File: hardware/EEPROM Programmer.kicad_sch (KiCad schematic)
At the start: 4 parts, among them U1 74HCT164, U2 74HCT164, U3 Teensy2.0_(Arduino)

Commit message: add power LED
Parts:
- added D1: LED, LED_THT:LED_D3.0mm, symbol Device:LED
- added R1: 2k2, Resistor_THT:R_Axial_DIN0207_L6.3mm_D2.5mm_P7.62mm_Horizontal, symbol Device:R
- renumbered 1 to 11
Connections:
- net +5V: now also R1.1
- net GND: now also D1.1 (K)
- new net: D1.2 (A), R1.2
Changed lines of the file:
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@@
     (pin "1")
+  )
+  (symbol (lib_id "Device:LED") (at 58.42 48.26 180) (unit 1)
+    (in_bom yes) (on_board yes) (fields_autoplaced)
+    (property "Reference" "D1" (id 0) (at 60.0075 40.64 0))
+    (property "Value" "LED" (id 1) (at 60.0075 43.18 0))
+    (property "Footprint" "LED_THT:LED_D3.0mm" (id 2) (at 58.42 48.26 0)
+      (effects (font (size 1.27 1.27)) hide)
+    )
+    (property "Datasheet" "~" (id 3) (at 58.42 48.26 0)
+      (effects (font (size 1.27 1.27)) hide)
+    )
+    (pin "1")
+    (pin "2")
   )
   (symbol (lib_id "power:+5V") (at 113.03 74.93 0) (unit 1)
@@
     (pin "9")
   )
+  (symbol (lib_id "power:GND") (at 62.23 48.26 90) (unit 1)
+    (in_bom yes) (on_board yes) (fields_autoplaced)
+    (property "Reference" "#PWR02" (id 0) (at 68.58 48.26 0)
+      (effects (font (size 1.27 1.27)) hide)
+    )
+    (property "Value" "GND" (id 1) (at 66.04 48.2599 90)
+      (effects (font (size 1.27 1.27)) (justify right))
+    )
+    (property "Footprint" "" (id 2) (at 62.23 48.26 0)
+      (effects (font (size 1.27 1.27)) hide)
+    )
+    (property "Datasheet" "" (id 3) (at 62.23 48.26 0)
+      (effects (font (size 1.27 1.27)) hide)
+    )
+    (pin "1")
+  )
   (symbol (lib_id "power:GND") (at 113.03 102.87 0) (unit 1)
     (in_bom yes) (on_board yes) (fields_autoplaced)
@@
     (pin "1")
   )
+  (symbol (lib_id "power:+5V") (at 46.99 48.26 90) (unit 1)
+    (in_bom yes) (on_board yes) (fields_autoplaced)
+    (property "Reference" "#PWR01" (id 0) (at 50.8 48.26 0)
+      (effects (font (size 1.27 1.27)) hide)
+    )
+    (property "Value" "+5V" (id 1) (at 43.18 48.2599 90)
+      (effects (font (size 1.27 1.27)) (justify left))
+    )
+    (property "Footprint" "" (id 2) (at 46.99 48.26 0)
+      (effects (font (size 1.27 1.27)) hide)
+    )
+    (property "Datasheet" "" (id 3) (at 46.99 48.26 0)
+      (effects (font (size 1.27 1.27)) hide)
+    )
+    (pin "1")
+  )
   (symbol (lib_id "28-6553-10_:28-6553-10_") (at 180.34 87.63 0) (unit 1)
-    (in_bom yes) (on_board yes) (fields_autoplaced)
-    (property "Reference" "1" (id 0) (at 232.41 78.2193 0))
-    (property "Value" "28-6553-10_" (id 1) (at 232.41 80.7593 0))
+    (in_bom yes) (on_board yes)
+    (property "Reference" "11" (id 0) (at 232.41 78.2193 0))
+    (property "Value" "28-6553-10_" (id 1) (at 232.41 81.28 0))
     (property "Footprint" "aries_zif:28655310" (id 2) (at 180.34 87.63 0)
       (effects (font (size 1.27 1.27)) hide)
@@
     )
     (property "Reference_1" "J" (id 4) (at 232.41 83.2993 0))
-    (property "Value_1" "28-6553-10_" (id 5) (at 232.41 85.8393 0))
+    (property "Value_1" "28-6553-10_" (id 5) (at 232.41 86.36 0))
     (property "Footprint_1" "28655310" (id 6) (at 224.79 177.47 0)
       (effects (font (size 1.27 1.27)) (justify left top) hide)
@@
     (pin "1")
   )
+  (symbol (lib_id "Device:R") (at 50.8 48.26 90) (unit 1)
+    (in_bom yes) (on_board yes) (fields_autoplaced)
+    (property "Reference" "R1" (id 0) (at 50.8 41.91 90))
+    (property "Value" "2k2" (id 1) (at 50.8 44.45 90))
+    (property "Footprint" "Resistor_THT:R_Axial_DIN0207_L6.3mm_D2.5mm_P7.62mm_Horizontal" (id 2) (at 50.8 50.038 90)
+      (effects (font (size 1.27 1.27)) hide)
+    )
+    (property "Datasheet" "~" (id 3) (at 50.8 48.26 0)
+      (effects (font (size 1.27 1.27)) hide)
+    )
+    (pin "1")
+    (pin "2")
+  )
   (sheet_instances
     (path "/" (page "1"))
   )
   (symbol_instances
+    (path "/c63c60b6-cef6-4c5a-8281-c9ca3487848c"
+      (reference "#PWR01") (unit 1) (value "+5V") (footprint "")
+    )
+    (path "/a79ec797-6aff-42a3-aa50-ffe5540c9212"
+      (reference "#PWR02") (unit 1) (value "GND") (footprint "")
+    )
     (path "/45c3618f-0671-416b-9a91-eff4d1eef6eb"
       (reference "#PWR0101") (unit 1) (value "GND") (footprint "")
@@
     )
     (path "/c9991c46-c0f1-40b8-b89b-d80d88dbb5f5"
-      (reference "1") (unit 1) (value "28-6553-10_") (footprint "aries_zif:28655310")
+      (reference "11") (unit 1) (value "28-6553-10_") (footprint "aries_zif:28655310")
+    )
+    (path "/79b34c4a-e5fe-43e9-8c64-054d107017f5"
+      (reference "D1") (unit 1) (value "LED") (footprint "LED_THT:LED_D3.0mm")
+    )
+    (path "/f85433e7-6fd8-482d-8fd4-e22dd35dd3ac"
+      (reference "R1") (unit 1) (value "2k2") (footprint "Resistor_THT:R_Axial_DIN0207_L6.3mm_D2.5mm_P7.62mm_Horizontal")
     )
     (path "/51f0c9ae-1fd9-4c54-9533-3dafdaf38498"

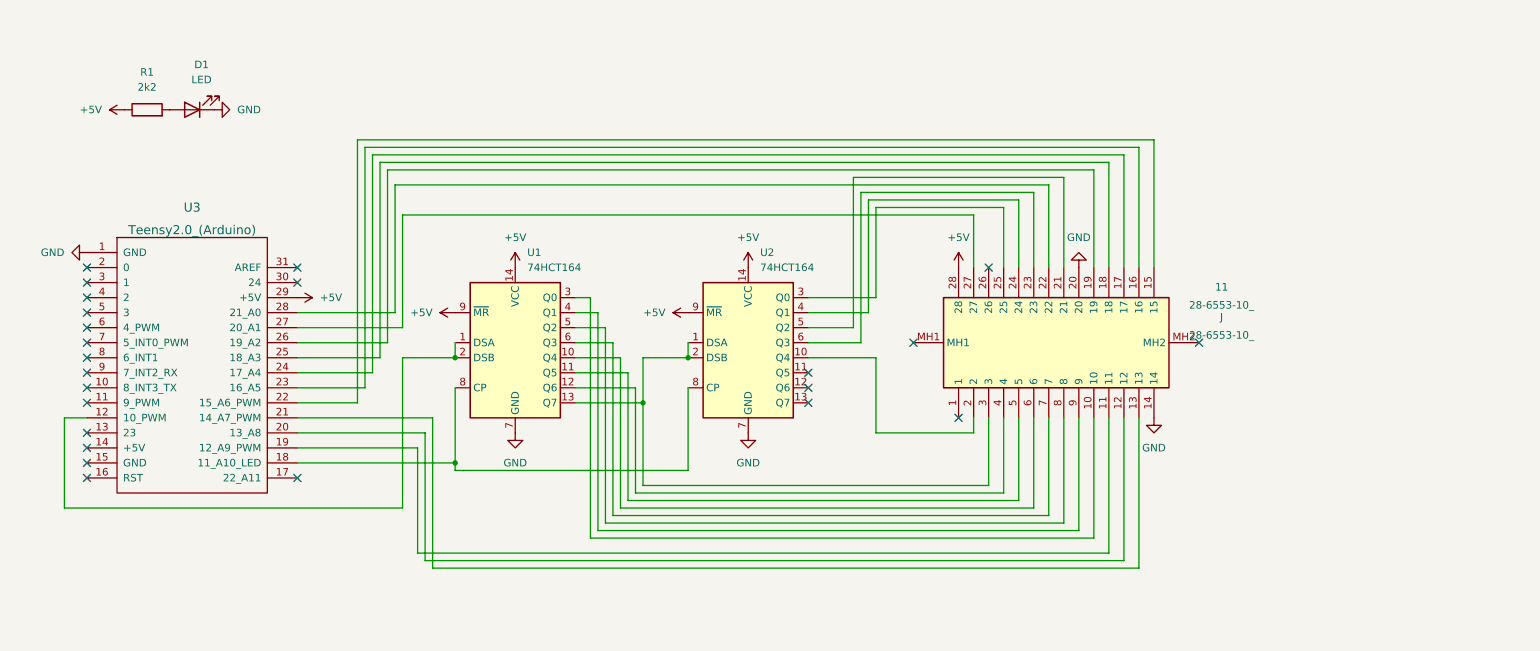
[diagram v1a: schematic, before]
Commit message: add Microchip 24LCxx support
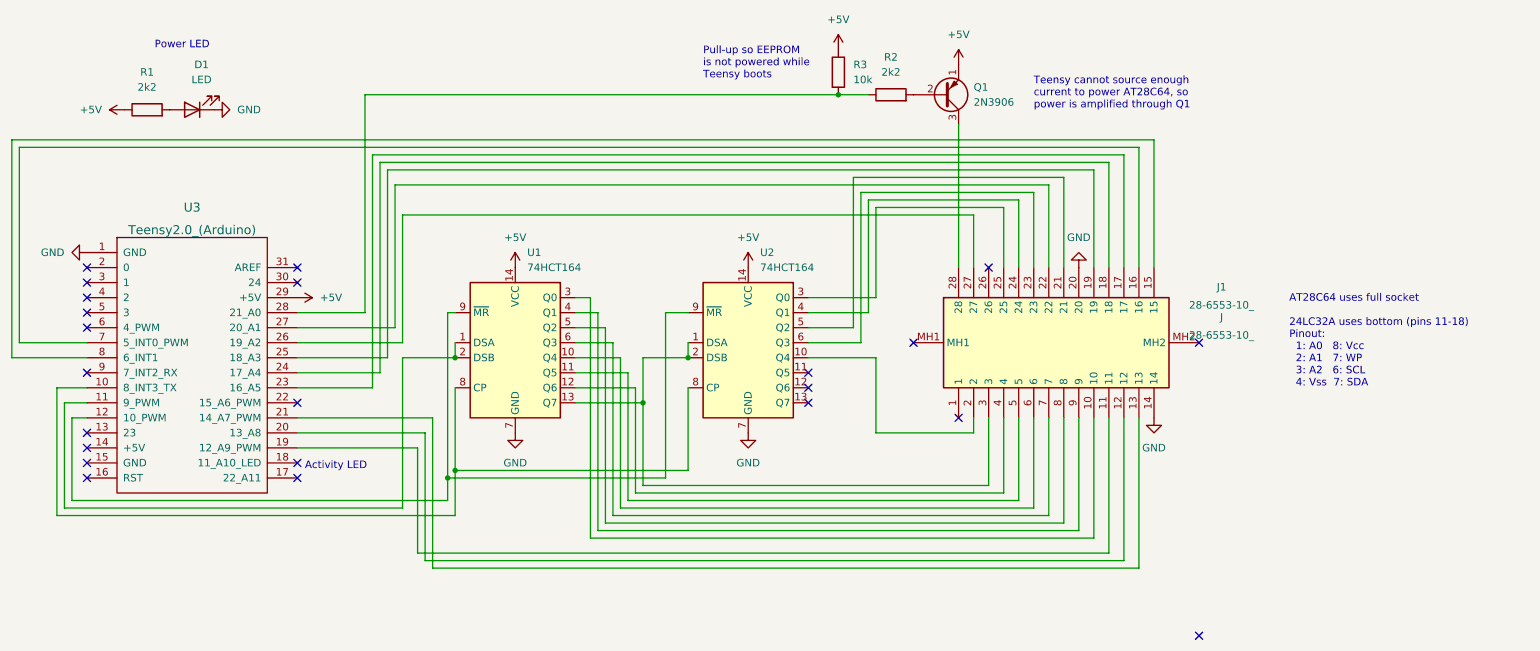
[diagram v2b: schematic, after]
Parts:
- added Q1: 2N3906, Package_TO_SOT_THT:TO-92_Inline, symbol Transistor_BJT:2N3906
- added R2: 2k2, Resistor_THT:R_Axial_DIN0207_L6.3mm_D2.5mm_P7.62mm_Horizontal, symbol Device:R
- added R3: 10k, Resistor_THT:R_Axial_DIN0207_L6.3mm_D2.5mm_P7.62mm_Horizontal, symbol Device:R
- renumbered 11 to J1
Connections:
- net +5V: now also Q1.1 (E), R3.1; no longer J1.28, U1.9 (~{MR}), U2.9 (~{MR})
- net at U1.1 (DSA), U1.2 (DSB): now also U3.11 (9_PWM); no longer U3.12 (10_PWM)
- net at U1.8 (CP), U2.8 (CP): now also U3.10 (8_INT3_TX); no longer U3.18 (11_A10_LED)
- net at U3.22 (15_A6_PWM): no longer J1.15
- net at U3.23 (16_A5): now also J1.17; no longer J1.16
- net at U3.24 (17_A4): now also J1.18; no longer J1.17
- net at U3.25 (18_A3): now also J1.19; no longer J1.18
- net at U3.26 (19_A2): now also J1.27; no longer J1.19
- net at U3.27 (20_A1): now also J1.22; no longer J1.27
- net at U3.28 (21_A0): now also R2.1, R3.2; no longer J1.22
- net at U3.7 (5_INT0_PWM): now also J1.16
- net at U3.8 (6_INT1): now also J1.15
- new net: Q1.2 (B), R2.2
- new net: U1.9 (~{MR}), U2.9 (~{MR}), U3.12 (10_PWM)
- new net: J1.28, Q1.3 (C)
- no-connect marks 24 -> 23
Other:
- note added: "AT28C64 uses full socket 24LC32A uses bottom (pins 11-18) Pinout: 1: A0 8: Vcc 2: A1 7: WP 3: A2 6: SCL 4: Vss 7: SDA"
- note added: "Activity LED"
- note added: "Power LED"
- note added: "Pull-up so EEPROM is not powered while Teensy boots"
- note added: "Teensy cannot source enough current to power AT28C64, so power is amplified through Q1"
